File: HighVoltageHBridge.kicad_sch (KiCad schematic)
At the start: 13 parts, among them J1 Screw_Terminal_01x02, J2 Conn_01x03_Socket, J3 Screw_Terminal_01x01, J4 Screw_Terminal_01x01, Q1 NMOS, Q2 NMOS, U1 SN74LVC1T45DCK, U2 DMC2700UDM-7, U3 Optocoupler_DC_PhotoNPN_AKEC, U4 Optocoupler_DC_PhotoNPN_AKEC

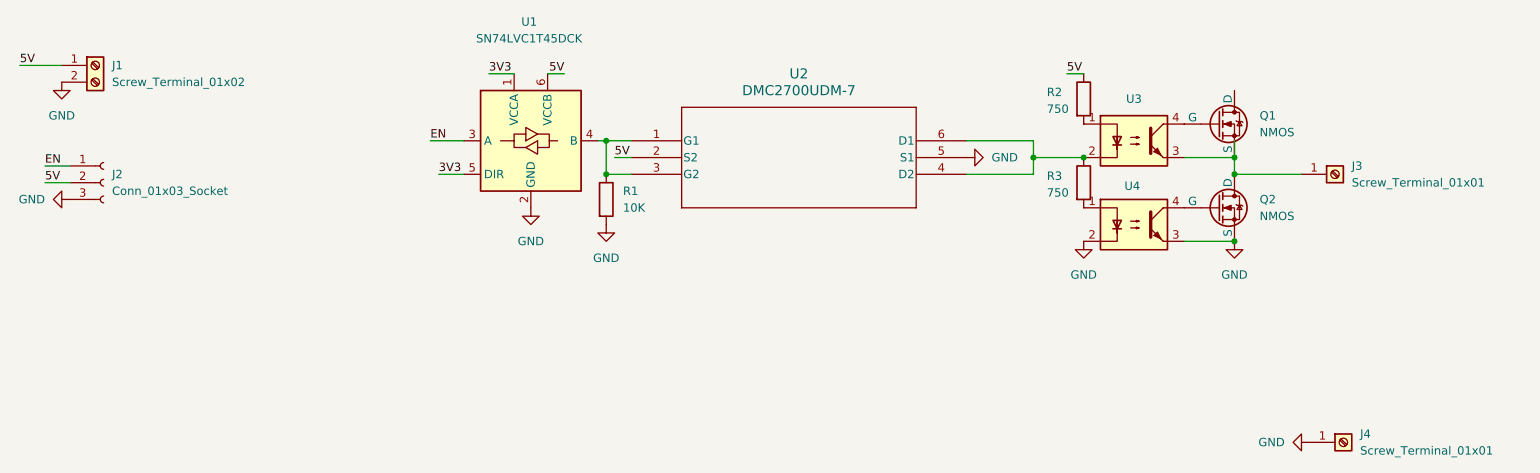
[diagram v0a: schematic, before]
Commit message: footprint issues solved
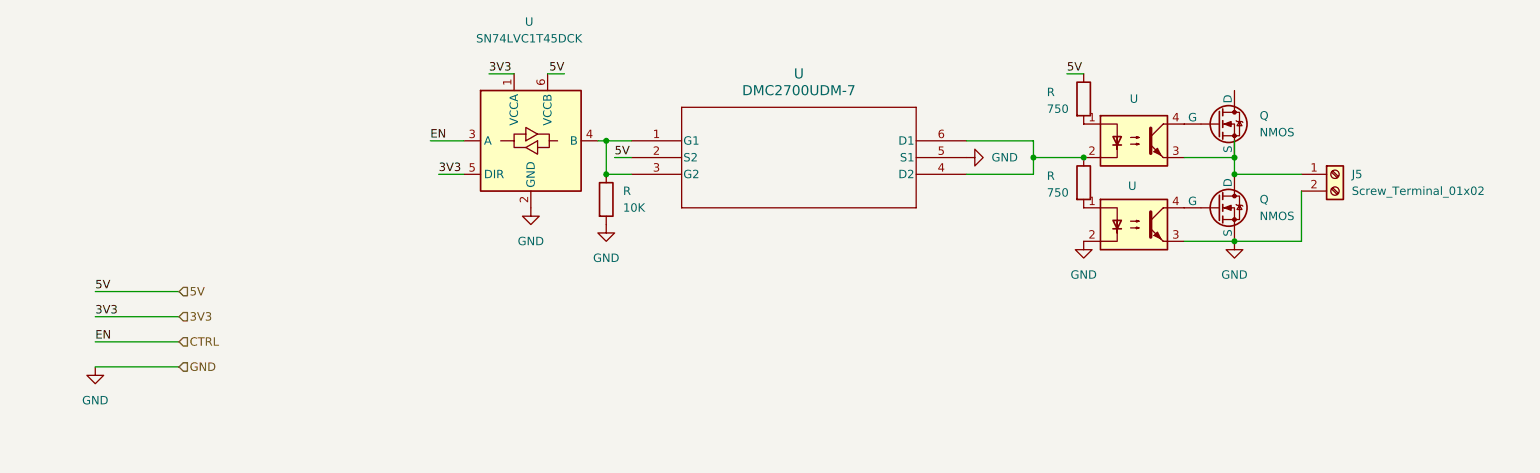
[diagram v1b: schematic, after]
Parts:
- removed J1: Screw_Terminal_01x02, TerminalBlock:TerminalBlock_MaiXu_MX126-5.0-02P_1x02_P5.00mm, symbol Connector:Screw_Terminal_01x02
- removed J2: Conn_01x03_Socket, Connector_PinSocket_2.54mm:PinSocket_1x03_P2.54mm_Vertical, symbol Connector:Conn_01x03_Socket
- removed J3, J4: Screw_Terminal_01x01, symbol Connector:Screw_Terminal_01x01
- added J5: Screw_Terminal_01x02, TerminalBlock:TerminalBlock_MaiXu_MX126-5.0-02P_1x02_P5.00mm, symbol Connector:Screw_Terminal_01x02
- U: renamed from U2; footprint DMC2700UDM:SOT26_DIO -> footprints:SOT26_DIO
- renumbered Q1 to Q, Q2 to Q, R2 to R, R3 to R, R1 to R, U1 to U, U3 to U, U4 to U
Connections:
- net GND: now also J5.2 (Pin_2)
- net at Q.1 (D), Q.3 (S), U.3: now also J5.1 (Pin_1)
- net EN renamed CTRL
